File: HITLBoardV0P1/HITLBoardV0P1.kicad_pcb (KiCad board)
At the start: 2 copper layers, 37 parts, among them U1 TMDX570LC43HDK_Connectors, U2 LAN8650B1-E/LMX, U3 LP38852MRX-ADJ/NOPB

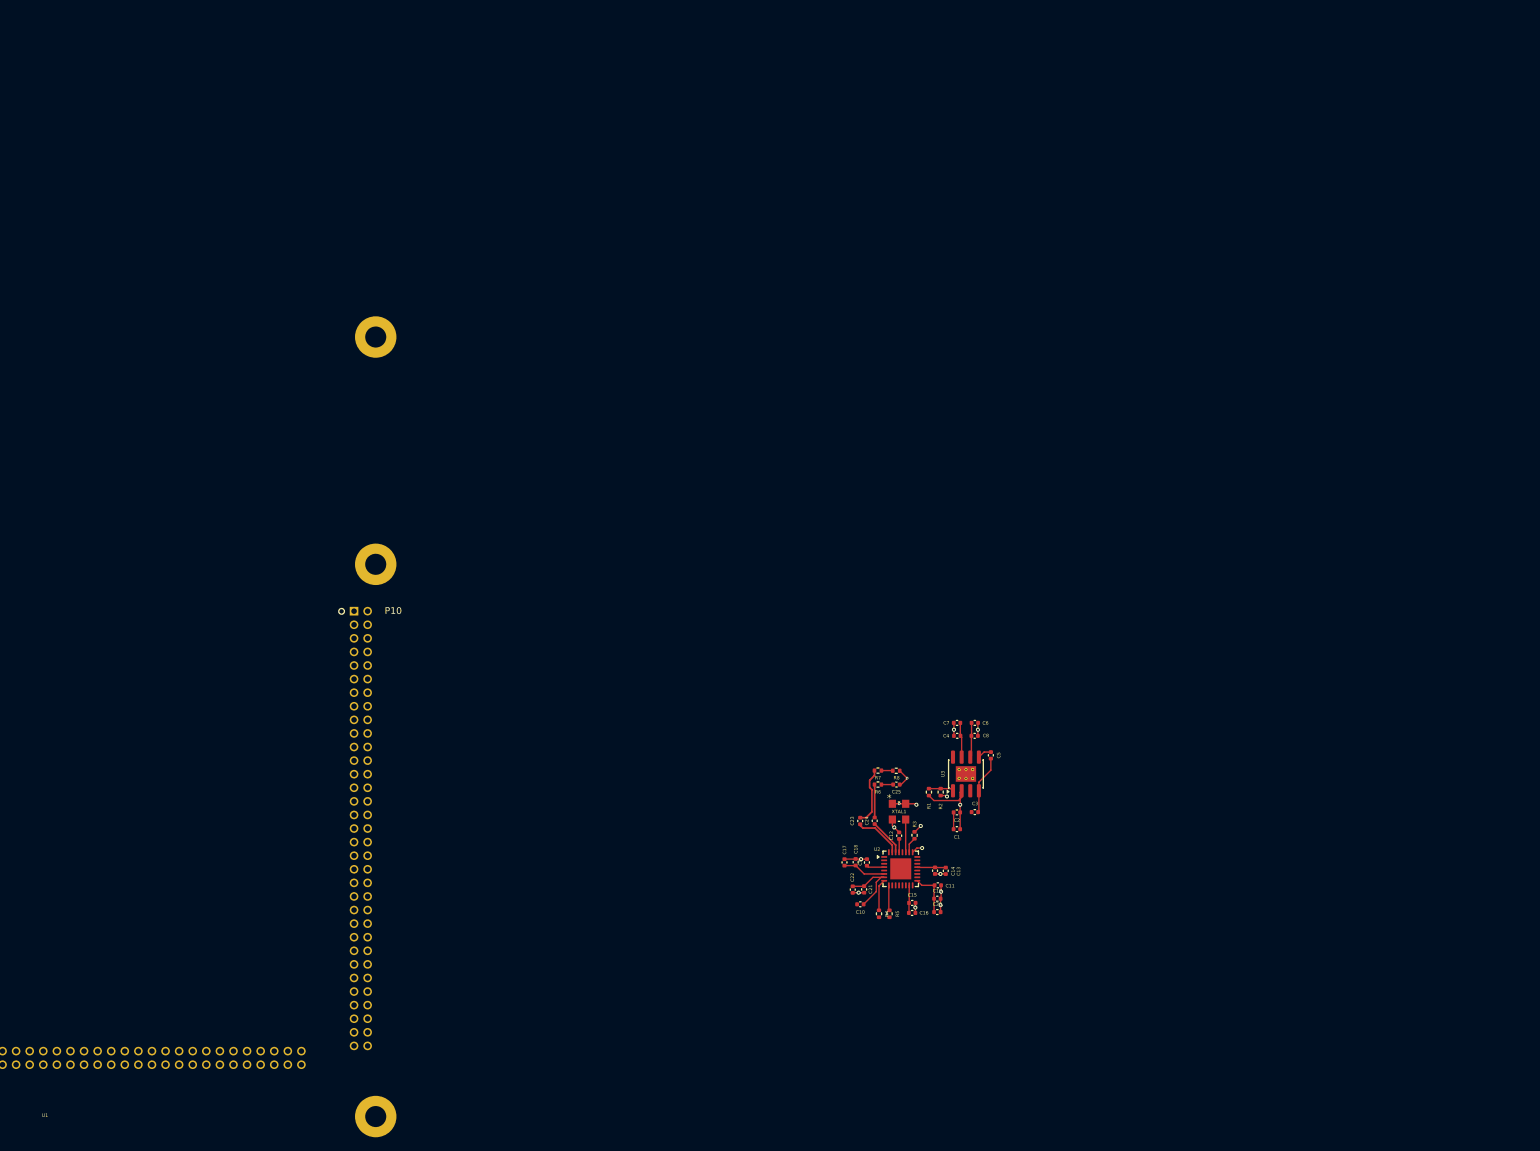
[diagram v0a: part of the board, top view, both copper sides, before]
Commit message: in progress, brute forced lan8650 layouts :( damn you kicad
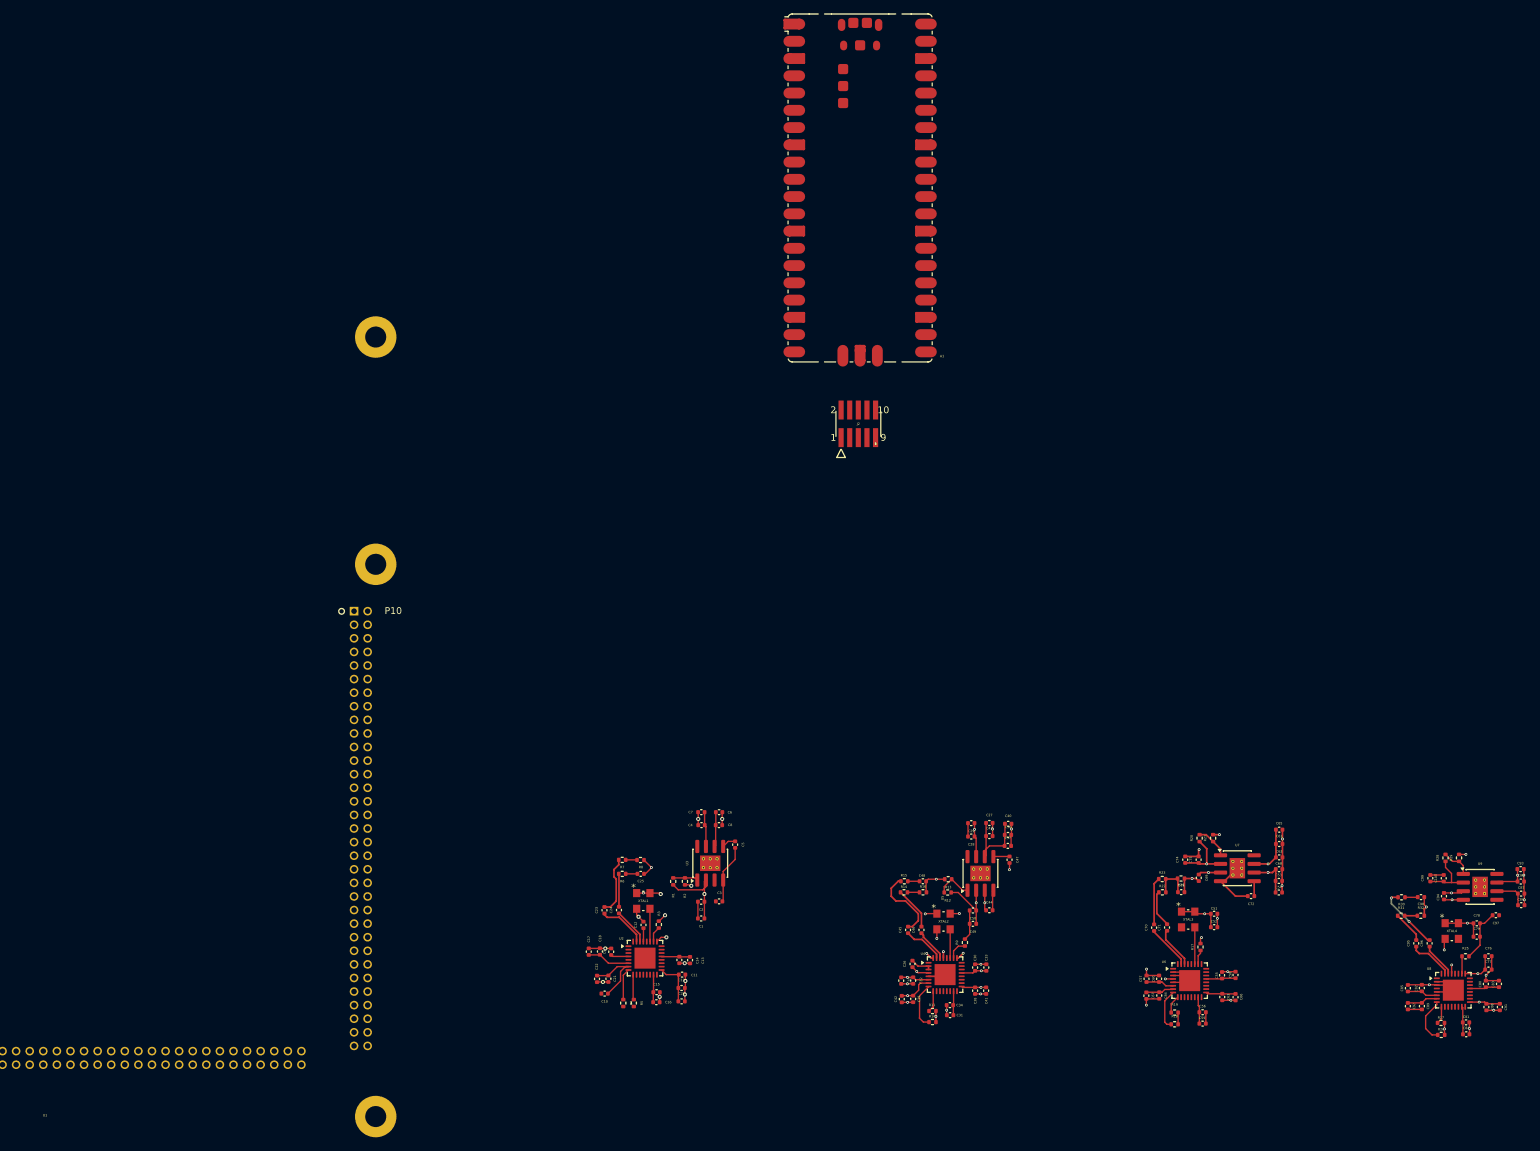
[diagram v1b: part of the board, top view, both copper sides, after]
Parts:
- added A1: RaspberryPi_Pico, Module:RaspberryPi_Pico_SMD, F.Cu at (295.7, 67.9)
- added C100: 1u, Capacitor_SMD:C_0402_1005Metric, F.Cu at (381.6, 169.6)
- added C26: 10u, Capacitor_SMD:C_0402_1005Metric, F.Cu at (303.4, 182.2)
- added C27: 10u, Capacitor_SMD:C_0402_1005Metric, F.Cu at (314.7, 161.4)
- added C28: 10u, Capacitor_SMD:C_0402_1005Metric, F.Cu at (312.1, 163.4)
- added C29: 10u, Capacitor_SMD:C_0402_1005Metric, F.Cu at (312.1, 161.5)
- added C30: 10n, Capacitor_SMD:C_0402_1005Metric, F.Cu at (312.6, 182.7)
- added C31: 10n, Capacitor_SMD:C_0402_1005Metric, F.Cu at (309.0, 189.7)
- added C32: 10n, Capacitor_SMD:C_0402_1005Metric, F.Cu at (303.5, 184.6)
- added C33: .1U, Capacitor_SMD:C_0402_1005Metric, F.Cu at (314.3, 182.7)
- added C34: .1U, Capacitor_SMD:C_0402_1005Metric, F.Cu at (308.9, 188.3)
- added C35: .1U, Capacitor_SMD:C_0402_1005Metric, F.Cu at (301.8, 184.6)
- added C36: 1u, Capacitor_SMD:C_0402_1005Metric, F.Cu at (317.5, 163.2)
- added C37: 1u, Capacitor_SMD:C_0402_1005Metric, F.Cu at (317.5, 164.8)
- added C38: 10n, Capacitor_SMD:C_0402_1005Metric, F.Cu at (312.6, 186.1)
- added C39: 10n, Capacitor_SMD:C_0402_1005Metric, F.Cu at (303.5, 187.3)
- added C40: 1u, Capacitor_SMD:C_0402_1005Metric, F.Cu at (317.5, 161.6)
- added C41: .1U, Capacitor_SMD:C_0402_1005Metric, F.Cu at (314.3, 186.1)
- added C42: .1U, Capacitor_SMD:C_0402_1005Metric, F.Cu at (301.9, 187.4)
- added C43: 1u, Capacitor_SMD:C_0402_1005Metric, F.Cu at (314.7, 163.4)
- added C44: 1u, Capacitor_SMD:C_0402_1005Metric, F.Cu at (314.7, 174.3)
- added C45: .1U, Capacitor_SMD:C_0402_1005Metric, F.Cu at (302.8, 177.2)
- added C46: .1U, Capacitor_SMD:C_0402_1005Metric, F.Cu at (304.7, 177.2)
- added C47: 1u, Capacitor_SMD:C_0402_1005Metric, F.Cu at (317.7, 166.8)
- added C48: .1U, Capacitor_SMD:C_0402_1005Metric, F.Cu at (305.0, 170.0)
- added C49: 100n, Capacitor_SMD:C_0402_1005Metric, F.Cu at (312.3, 176.3)
- added C50: 1u, Capacitor_SMD:C_0402_1005Metric, F.Cu at (312.3, 174.3)
- added C51: 10u, Capacitor_SMD:C_0402_1005Metric, F.Cu at (347.8, 174.8)
- added C52: 10u, Capacitor_SMD:C_0402_1005Metric, F.Cu at (347.8, 176.8)
- added C53: 10u, Capacitor_SMD:C_0402_1005Metric, F.Cu at (357.4, 170.0)
- added C54: 10u, Capacitor_SMD:C_0402_1005Metric, F.Cu at (357.4, 171.7)
- added C55: 10n, Capacitor_SMD:C_0402_1005Metric, F.Cu at (349.0, 183.9)
- added C56: 10n, Capacitor_SMD:C_0402_1005Metric, F.Cu at (346.1, 189.3)
- added C57: 10n, Capacitor_SMD:C_0402_1005Metric, F.Cu at (337.9, 184.4)
- added C58: .1U, Capacitor_SMD:C_0402_1005Metric, F.Cu at (351.0, 183.8)
- added C59: .1U, Capacitor_SMD:C_0402_1005Metric, F.Cu at (346.1, 191.0)
- added C60: .1U, Capacitor_SMD:C_0402_1005Metric, F.Cu at (339.7, 184.4)
- added C61: 1u, Capacitor_SMD:C_0402_1005Metric, F.Cu at (357.4, 164.5)
- added C62: 1u, Capacitor_SMD:C_0402_1005Metric, F.Cu at (357.4, 166.5)
- added C63: 10n, Capacitor_SMD:C_0402_1005Metric, F.Cu at (349.0, 187.1)
- added C64: 10n, Capacitor_SMD:C_0402_1005Metric, F.Cu at (339.8, 186.8)
- added C65: 1u, Capacitor_SMD:C_0402_1005Metric, F.Cu at (357.4, 162.4)
- added C66: .1U, Capacitor_SMD:C_0402_1005Metric, F.Cu at (351.0, 187.1)
- added C67: .1U, Capacitor_SMD:C_0402_1005Metric, F.Cu at (337.9, 186.9)
- added C68: 1u, Capacitor_SMD:C_0402_1005Metric, F.Cu at (357.4, 168.2)
- added C69: 1u, Capacitor_SMD:C_0402_1005Metric, F.Cu at (345.6, 169.5)
- added C70: .1U, Capacitor_SMD:C_0402_1005Metric, F.Cu at (339.0, 176.8)
- added C71: .1U, Capacitor_SMD:C_0402_1005Metric, F.Cu at (340.9, 176.8)
- added C72: 1u, Capacitor_SMD:C_0402_1005Metric, F.Cu at (353.3, 172.2)
- added C73: .1U, Capacitor_SMD:C_0402_1005Metric, F.Cu at (343.0, 171.6)
- added C74: 100n, Capacitor_SMD:C_0402_1005Metric, F.Cu at (343.6, 166.8)
- added C75: 1u, Capacitor_SMD:C_0402_1005Metric, F.Cu at (345.6, 166.8)
- added C76: 10u, Capacitor_SMD:C_0402_1005Metric, F.Cu at (388.2, 181.0)
- added C77: 10u, Capacitor_SMD:C_0402_1005Metric, F.Cu at (388.2, 183.0)
- added C78: 10u, Capacitor_SMD:C_0402_1005Metric, F.Cu at (386.5, 176.2)
- added C79: 10u, Capacitor_SMD:C_0402_1005Metric, F.Cu at (386.5, 178.2)
- added C80: 10n, Capacitor_SMD:C_0402_1005Metric, F.Cu at (387.8, 185.1)
- added C81: 10n, Capacitor_SMD:C_0402_1005Metric, F.Cu at (384.9, 190.8)
- added C82: 10n, Capacitor_SMD:C_0402_1005Metric, F.Cu at (378.4, 185.7)
- added C83: .1U, Capacitor_SMD:C_0402_1005Metric, F.Cu at (389.8, 185.1)
- added C84: .1U, Capacitor_SMD:C_0402_1005Metric, F.Cu at (384.9, 192.5)
- added C85: .1U, Capacitor_SMD:C_0402_1005Metric, F.Cu at (376.4, 185.8)
- added C86: 1u, Capacitor_SMD:C_0402_1005Metric, F.Cu at (393.1, 173.5)
- added C87: 1u, Capacitor_SMD:C_0402_1005Metric, F.Cu at (393.0, 171.8)
- added C88: 10n, Capacitor_SMD:C_0402_1005Metric, F.Cu at (387.9, 188.5)
- added C89: 10n, Capacitor_SMD:C_0402_1005Metric, F.Cu at (378.4, 188.4)
- added C90: 1u, Capacitor_SMD:C_0402_1005Metric, F.Cu at (393.0, 170.1)
- added C91: .1U, Capacitor_SMD:C_0402_1005Metric, F.Cu at (389.9, 188.5)
- added C92: .1U, Capacitor_SMD:C_0402_1005Metric, F.Cu at (376.4, 188.4)
- added C93: 1u, Capacitor_SMD:C_0402_1005Metric, F.Cu at (393.0, 168.2)
- added C94: 1u, Capacitor_SMD:C_0402_1005Metric, F.Cu at (381.7, 172.2)
- added C95: .1U, Capacitor_SMD:C_0402_1005Metric, F.Cu at (377.6, 179.2)
- added C96: .1U, Capacitor_SMD:C_0402_1005Metric, F.Cu at (379.6, 179.2)
- added C97: 1u, Capacitor_SMD:C_0402_1005Metric, F.Cu at (389.3, 175.0)
- added C98: .1U, Capacitor_SMD:C_0402_1005Metric, F.Cu at (378.3, 172.3)
- added C99: 100n, Capacitor_SMD:C_0402_1005Metric, F.Cu at (379.7, 169.6)
- added J2: FTSH-105-01-L-DV, GaladyneConnectorFootprintsLibrary:CON10_2X5_DU_FTSH_SAI, F.Cu at (295.5, 102.7)
- added R10: 10K, Resistor_SMD:R_0402_1005Metric, F.Cu at (306.4, 190.7)
- added R11: 10K, Resistor_SMD:R_0402_1005Metric, F.Cu at (306.4, 189.1)
- added R12: 2.94K, Resistor_SMD:R_0402_1005Metric, F.Cu at (308.6, 171.7)
- added R13: 1.13K, Resistor_SMD:R_0402_1005Metric, F.Cu at (308.7, 169.7)
- added R14: 49.9K, Resistor_SMD:R_0402_1005Metric, F.Cu at (302.2, 171.6)
- added R15: 49.9K, Resistor_SMD:R_0402_1005Metric, F.Cu at (302.2, 170.0)
- added R16: 100K, Resistor_SMD:R_0402_1005Metric, F.Cu at (305.0, 171.6)
- added R17: 12.4K, Resistor_SMD:R_0402_1005Metric, F.Cu at (345.8, 179.7)
- added R18: 10K, Resistor_SMD:R_0402_1005Metric, F.Cu at (342.0, 191.1)
- added R19: 10K, Resistor_SMD:R_0402_1005Metric, F.Cu at (342.0, 189.3)
- added R20: 2.94K, Resistor_SMD:R_0402_1005Metric, F.Cu at (345.7, 163.7)
- added R21: 1.13K, Resistor_SMD:R_0402_1005Metric, F.Cu at (347.7, 163.7)
- added R22: 49.9K, Resistor_SMD:R_0402_1005Metric, F.Cu at (340.2, 171.6)
- added R23: 49.9K, Resistor_SMD:R_0402_1005Metric, F.Cu at (340.2, 169.7)
- added R24: 100K, Resistor_SMD:R_0402_1005Metric, F.Cu at (343.0, 169.6)
- added R25: 12.4K, Resistor_SMD:R_0402_1005Metric, F.Cu at (384.8, 181.1)
- added R26: 10K, Resistor_SMD:R_0402_1005Metric, F.Cu at (381.3, 192.6)
- added R27: 10K, Resistor_SMD:R_0402_1005Metric, F.Cu at (381.2, 190.9)
- added R28: 2.94K, Resistor_SMD:R_0402_1005Metric, F.Cu at (381.9, 166.6)
- added R29: 1.13K, Resistor_SMD:R_0402_1005Metric, F.Cu at (383.9, 166.6)
- added R30: 49.9K, Resistor_SMD:R_0402_1005Metric, F.Cu at (375.4, 172.4)
- added R31: 49.9K, Resistor_SMD:R_0402_1005Metric, F.Cu at (375.4, 175.1)
- added R32: 100K, Resistor_SMD:R_0402_1005Metric, F.Cu at (378.3, 175.1)
- added R9: 12.4K, Resistor_SMD:R_0402_1005Metric, F.Cu at (311.1, 179.0)
- added U4: LAN8650B1-E/LMX, Package_DFN_QFN:QFN-32-1EP_5x5mm_P0.5mm_EP3.1x3.1mm, F.Cu at (308.2, 183.8)
- added U5: LP38852MRX-ADJ/NOPB, Package_SO:SOIC-8-1EP_3.9x4.9mm_P1.27mm_EP2.29x3mm_ThermalVias, F.Cu at (313.4, 168.9)
- added U6: LAN8650B1-E/LMX, Package_DFN_QFN:QFN-32-1EP_5x5mm_P0.5mm_EP3.1x3.1mm, F.Cu at (344.2, 184.6)
- added U7: LP38852MRX-ADJ/NOPB, Package_SO:SOIC-8-1EP_3.9x4.9mm_P1.27mm_EP2.29x3mm_ThermalVias, F.Cu at (351.3, 168.1)
- added U8: LAN8650B1-E/LMX, Package_DFN_QFN:QFN-32-1EP_5x5mm_P0.5mm_EP3.1x3.1mm, F.Cu at (383.1, 186.1)
- added U9: LP38852MRX-ADJ/NOPB, Package_SO:SOIC-8-1EP_3.9x4.9mm_P1.27mm_EP2.29x3mm_ThermalVias, F.Cu at (387.0, 170.8)
- added XTAL2: ECS-2520S33-250-FN-TR, GaladyneOscillatorFootprintsLibrary:ECS-2520S_ECS, F.Cu at (308.0, 175.9)
- added XTAL3: ECS-2520S33-250-FN-TR, GaladyneOscillatorFootprintsLibrary:ECS-2520S_ECS, F.Cu at (344.0, 175.6)
- added XTAL4: ECS-2520S33-250-FN-TR, GaladyneOscillatorFootprintsLibrary:ECS-2520S_ECS, F.Cu at (382.8, 177.3)
- C1: value 100n -> 10u
- C10, C9: value 10u -> .1U
- C11, C12: value 10u -> 1u
- C14: value .1U -> 10n
- C15, C19: value 10n -> 1u
- C17, C21: value 10n -> .1U
- C18, C22, C25: value .1U -> 1u
- C2, C3, C4: value 1u -> 10u
- C24: value .1U -> 100n
- C5, C6, C7: value 1u -> 10n
- C8: value 1u -> .1U
- R1: value 2.94K -> 12.4K
- R2: value 1.13K -> 10K
- R3: value 12.4K -> 10K
- R4: value 10K -> 2.94K
- R5: value 10K -> 1.13K
- moved C18 39.9 mm to (257.4, 180.4)
- moved C25 39.9 mm to (263.4, 168.9)
- moved R6 39.9 mm to (260.7, 168.9)
- moved R4 39.9 mm to (260.9, 187.9)
- moved R5 39.9 mm to (262.4, 187.9)
- moved C1 39.9 mm to (272.3, 175.5)
- moved C10 39.9 mm to (258.1, 186.6)
- moved C11 39.9 mm to (269.5, 183.8)
- moved C13 39.9 mm to (270.7, 181.6)
- moved C14 39.9 mm to (269.1, 181.6)
- moved C15 39.9 mm to (265.8, 186.3)
- moved C17 39.9 mm to (255.8, 180.4)
- moved C19 39.9 mm to (269.4, 185.7)
- moved C2 39.9 mm to (272.3, 173.0)
- moved C20 39.9 mm to (269.4, 187.7)
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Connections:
- C1 pad 1: /Ethernet/1V8_U2 -> +3V3
- C13 pad 1: /Ethernet/1V8_U2 -> +3V3
- C14 pad 1: /Ethernet/1V8_U2 -> +3V3
- C15 pad 1: /Ethernet/1V8_U2 -> +3V3
- C16 pad 1: /Ethernet/1V8_U2 -> +3V3
- C17 pad 1: /Ethernet/1V8_U2 -> +3V3
- C18 pad 1: /Ethernet/1V8_U2 -> +3V3
- C19 pad 1: +3V3 -> +5V
- C2 pad 1: /Ethernet/1V8_U2 -> +3V3
- C20 pad 1: +3V3 -> /Ethernet/TRXN
- C20 pad 2: GND -> /Ethernet/ETH_10T1S_TRXN
- C21 pad 1: +3V3 -> /Ethernet/TRXP
- C21 pad 2: GND -> /Ethernet/ETH_10T1S_TRXP
- C22 pad 1: +3V3 -> /Ethernet/U3_SS
- C23 pad 1: /Ethernet/TRXN_N -> GND
- C23 pad 2: /Ethernet/ETH_10T1S_TRXN_N -> Net-(C23-Pad2)
- C24 pad 1: /Ethernet/TRXP_P -> /Ethernet/1V8_U2
- C24 pad 2: /Ethernet/ETH_10T1S_TRXP_P -> GND
- C25 pad 1: GND -> /Ethernet/1V8_U2
- C25 pad 2: Net-(C25-Pad2) -> GND
- C3 pad 1: +5V -> +3V3
- C5 pad 1: /Ethernet/U3_SS -> +3V3
- R1 pad 1: /Ethernet/1V8_U2 -> /Ethernet/BIAS
- R1 pad 2: /Ethernet/U3_ADJ -> GND
- R2 pad 1: /Ethernet/U3_ADJ -> /Ethernet/RESET_N
- R2 pad 2: GND -> +3V3
- R3 pad 1: /Ethernet/BIAS -> /Ethernet/IRQ_N
- R3 pad 2: GND -> +3V3
- R4 pad 1: /Ethernet/RESET_N -> /Ethernet/1V8_U2
- R4 pad 2: +3V3 -> /Ethernet/U3_ADJ
- R5 pad 1: /Ethernet/IRQ_N -> /Ethernet/U3_ADJ
- R5 pad 2: +3V3 -> GND
- R6 pad 1: /Ethernet/ETH_10T1S_TRXP_P -> /Ethernet/ETH_10T1S_TRXP
- R6 pad 2: Net-(C25-Pad2) -> Net-(C23-Pad2)
- R7 pad 1: /Ethernet/ETH_10T1S_TRXN_N -> /Ethernet/ETH_10T1S_TRXN
- R7 pad 2: Net-(C25-Pad2) -> Net-(C23-Pad2)
- R8 pad 1: Net-(C25-Pad2) -> Net-(C23-Pad2)
- U1 pad P10-1: unconnected-(U1B-EXP_12V-PadP10-1) -> +12V
- U1 pad P10-29: unconnected-(U1B-GND-PadP10-29) -> GND
- U1 pad P10-30: unconnected-(U1B-GND-PadP10-30) -> GND
- U1 pad P10-39: unconnected-(U1B-GND-PadP10-39) -> GND
- U1 pad P10-40: unconnected-(U1B-GND-PadP10-40) -> GND
- U1 pad P10-57: unconnected-(U1B-GND-PadP10-57) -> GND
- U1 pad P10-58: unconnected-(U1B-GND-PadP10-58) -> GND
- U1 pad P10-65: unconnected-(U1B-EXP_12V-PadP10-65) -> +12V
- U1 pad P10-66: unconnected-(U1B-GND-PadP10-66) -> GND
- U1 pad P11-1: unconnected-(U1C-EXP_12V-PadP11-1) -> +12V
- U1 pad P11-19: unconnected-(U1C-GIOA_1-PadP11-19) -> /TMDX_Breakout/GIOA_1
- U1 pad P11-21: unconnected-(U1C-GIOA_3-PadP11-21) -> /TMDX_Breakout/GIOA_3
- U1 pad P11-23: unconnected-(U1C-GIOA_5-PadP11-23) -> /TMDX_Breakout/GIOA_5
- U1 pad P11-25: unconnected-(U1C-GIOA_7-PadP11-25) -> /TMDX_Breakout/GIOA_7
- U1 pad P11-27: unconnected-(U1C-GIOB_1-PadP11-27) -> /TMDX_Breakout/GIOB_1
- U1 pad P11-29: unconnected-(U1C-GIOB_3-PadP11-29) -> /TMDX_Breakout/GIOB_3
- U1 pad P11-3: unconnected-(U1C-EXP_12V-PadP11-3) -> +12V
- U1 pad P11-31: unconnected-(U1C-GIOB_5-PadP11-31) -> /TMDX_Breakout/GIOB_5
- U1 pad P9-1: unconnected-(U1A-EXP_12V-PadP9-1) -> +12V
- U1 pad P9-13: unconnected-(U1A-GND-PadP9-13) -> GND
- U1 pad P9-14: unconnected-(U1A-GND-PadP9-14) -> GND
- U1 pad P9-2: unconnected-(U1A-GND-PadP9-2) -> GND
- U1 pad P9-29: unconnected-(U1A-GND-PadP9-29) -> GND
- U1 pad P9-3: unconnected-(U1A-EXP_12V-PadP9-3) -> +12V
- U1 pad P9-30: unconnected-(U1A-GND-PadP9-30) -> GND
- U1 pad P9-39: unconnected-(U1A-GND-PadP9-39) -> GND
- U1 pad P9-4: unconnected-(U1A-GND-PadP9-4) -> GND
- U1 pad P9-40: unconnected-(U1A-GND-PadP9-40) -> GND
- U1 pad P9-49: unconnected-(U1A-GND-PadP9-49) -> GND
- U1 pad P9-50: unconnected-(U1A-GND-PadP9-50) -> GND
- U1 pad P9-59: unconnected-(U1A-GND-PadP9-59) -> GND
- U1 pad P9-65: unconnected-(U1A-EXP_12V-PadP9-65) -> +12V
- U1 pad P9-66: unconnected-(U1A-GND-PadP9-66) -> GND
- U2 pad 30: /Ethernet/TRXP_P -> /Ethernet/TRXP
- U2 pad 31: /Ethernet/TRXN_N -> /Ethernet/TRXN
- U3 pad 9: GND -> /Ethernet/U3_DAP
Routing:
- net GND: track 34.8 -> 164.7 mm, vias 12 -> 41
- net +3V3: track 37.6 -> 141.3 mm, vias 3 -> 24
- net (no net): track 0.00 -> 27.8 mm
- net /ethernet3/1V8: track 0.00 -> 21.5 mm, vias 0 -> 1
- net /ethernet4/1V8: track 0.00 -> 21.4 mm
- net /Ethernet2/1V8: track 0.00 -> 21.2 mm, vias 0 -> 3
- net /Ethernet2/ETH_10T1S_TRXN: track 0.00 -> 11.0 mm
- net /ethernet4/ETH_10T1S_TRXP: track 0.00 -> 9.73 mm, vias 0 -> 2
- net +5V: track 0.00 -> 9.30 mm, vias 0 -> 3
- net /Ethernet/ETH_10T1S_TRXN_N: track 8.59 -> 0.00 mm
- net /Ethernet/TRXN_N: track 7.15 -> 0.00 mm
- net /ethernet3/ETH_10T1S_TRXN: track 0.00 -> 6.96 mm
- net /LAN_RESET_N_1: track 0.00 -> 6.87 mm
- net /ethernet4/RESET_N: track 0.00 -> 6.74 mm
- net /ethernet3/TRXN: track 0.00 -> 6.53 mm
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
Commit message: update
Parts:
- added C101: 100p, Capacitor_SMD:C_0402_1005Metric, F.Cu at (343.1, 124.1)
- added C102: 0.1u, Capacitor_SMD:C_0402_1005Metric, F.Cu at (341.1, 124.1)
- added C103: 0.1u, Capacitor_SMD:C_0402_1005Metric, F.Cu at (337.3, 129.1)
- added C104: 0.1u, Capacitor_SMD:C_0402_1005Metric, F.Cu at (329.3, 132.6)
- added C105: 0.1u, Capacitor_SMD:C_0402_1005Metric, F.Cu at (335.0, 132.4)
- added C106: 0.1u, Capacitor_SMD:C_0402_1005Metric, F.Cu at (342.8, 138.5)
- added C107: 0.1u, Capacitor_SMD:C_0402_1005Metric, F.Cu at (353.6, 134.8)
- added R33: 10, Resistor_SMD:R_1206_3216Metric, F.Cu at (345.9, 125.0)
- added R34: 15, Resistor_SMD:R_1206_3216Metric, F.Cu at (352.6, 132.2)
- added R35: 15K, Resistor_SMD:R_0402_1005Metric, F.Cu at (345.9, 138.7)
- added U10: DAC7750IPWPR, GaladyneIntegratedCircuitsFootprintsLibrary:PWP24_TEX, F.Cu at (343.0, 132.5)
- added U11: NC7SZ04P5X, GaladyneIntegratedCircuitsFootprintsLibrary:SC-88A-5_1P35X2P2_ONS, F.Cu at (328.8, 135.3)
- added U12: SN74LVC1G08DCKR, GaladyneIntegratedCircuitsFootprintsLibrary:DCK5, F.Cu at (334.1, 135.3)
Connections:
- net /Ethernet2/ETH_10T1S_TRXN renamed /ETH_10T1S_A_TRXN
- net /Ethernet2/ETH_10T1S_TRXP renamed /ETH_10T1S_A_TRXP
- C70 pad 2: /ethernet3/ETH_10T1S_TRXN -> /ETH_10T1S_B_TRXN
- C71 pad 2: /ethernet3/ETH_10T1S_TRXP -> /ETH_10T1S_B_TRXP
- C95 pad 2: /ethernet4/ETH_10T1S_TRXN -> /ETH_10T1S_B_TRXN
- C96 pad 2: /ethernet4/ETH_10T1S_TRXP -> /ETH_10T1S_B_TRXP
- R22 pad 1: /ethernet3/ETH_10T1S_TRXP -> /ETH_10T1S_B_TRXP
- R23 pad 1: /ethernet3/ETH_10T1S_TRXN -> /ETH_10T1S_B_TRXN
- R30 pad 1: /ethernet4/ETH_10T1S_TRXP -> /ETH_10T1S_B_TRXP
- R31 pad 1: /ethernet4/ETH_10T1S_TRXN -> /ETH_10T1S_B_TRXN
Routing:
- net /ETH_10T1S_B_TRXP: track 0.00 -> 15.2 mm, vias 0 -> 2
- net GND: track 164.7 -> 179.6 mm, vias 41 -> 50
- net /ETH_10T1S_B_TRXN: track 0.00 -> 11.7 mm
- net /ethernet4/ETH_10T1S_TRXP: track 9.73 -> 0.00 mm, vias 2 -> 0
- net +3.3VP: track 0.00 -> 8.27 mm, vias 0 -> 2
- net /ethernet3/ETH_10T1S_TRXN: track 6.96 -> 0.00 mm
- net /DAC/SCLK_AND_LATCH_N: track 0.00 -> 5.97 mm
- net /DAC/REFOUT: track 0.00 -> 5.56 mm
- net /ethernet3/ETH_10T1S_TRXP: track 5.45 -> 0.00 mm
- net /DAC/IOUT: track 0.00 -> 5.21 mm
- net +12V: track 0.00 -> 4.84 mm
- net /ethernet4/ETH_10T1S_TRXN: track 4.71 -> 0.00 mm
- net /DAC/LATCH_N: track 0.00 -> 3.84 mm
- net /DAC/CURRENT_OUT: track 0.00 -> 2.62 mm
- net /DAC/AVDD: track 0.00 -> 2.45 mm
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
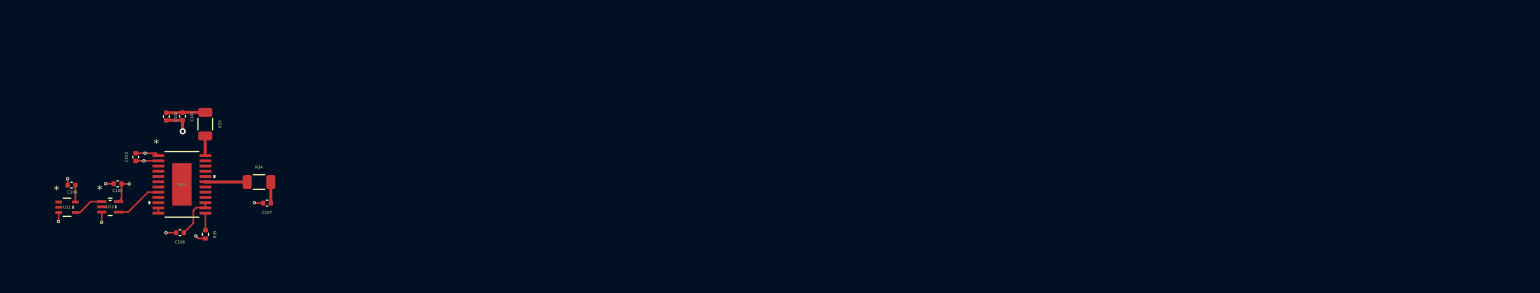
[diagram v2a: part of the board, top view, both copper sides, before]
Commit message: UPDATE IN PROGRESS, 4 DACS ADDED AND INITIAL ROUTED IN PCB
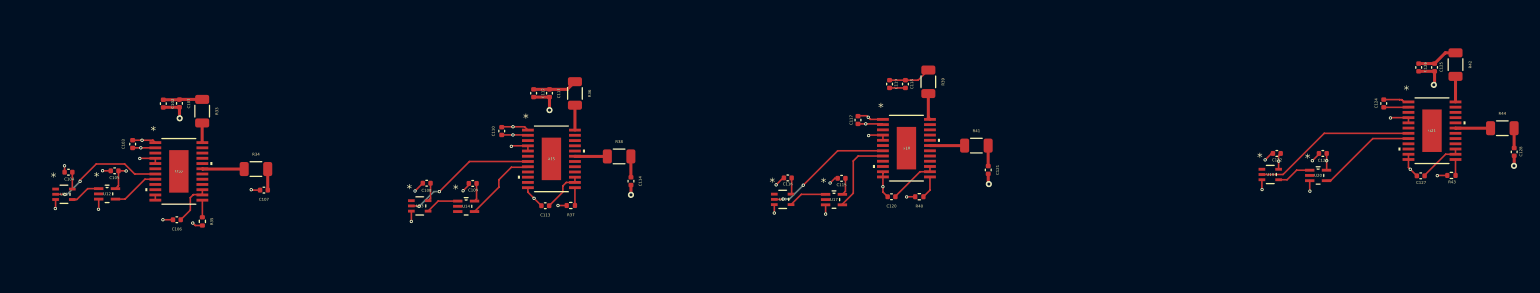
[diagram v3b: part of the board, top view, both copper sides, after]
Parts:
- added C108: 0.1u, Capacitor_SMD:C_0402_1005Metric, F.Cu at (373.4, 132.4)
- added C109: 0.1u, Capacitor_SMD:C_0402_1005Metric, F.Cu at (379.1, 132.4)
- added C110: 0.1u, Capacitor_SMD:C_0402_1005Metric, F.Cu at (382.8, 125.9)
- added C111: 100p, Capacitor_SMD:C_0402_1005Metric, F.Cu at (388.7, 121.2)
- added C112: 0.1u, Capacitor_SMD:C_0402_1005Metric, F.Cu at (386.7, 121.2)
- added C113: 0.1u, Capacitor_SMD:C_0402_1005Metric, F.Cu at (388.2, 135.2)
- added C114: 0.1u, Capacitor_SMD:C_0402_1005Metric, F.Cu at (398.8, 132.1)
- added C115: 0.1u, Capacitor_SMD:C_0402_1005Metric, F.Cu at (425.0, 131.8)
- added C116: 0.1u, Capacitor_SMD:C_0402_1005Metric, F.Cu at (418.3, 131.7)
- added C117: 0.1u, Capacitor_SMD:C_0402_1005Metric, F.Cu at (427.0, 124.5)
- added C118: 100p, Capacitor_SMD:C_0402_1005Metric, F.Cu at (432.9, 120.0)
- added C119: 0.1u, Capacitor_SMD:C_0402_1005Metric, F.Cu at (430.9, 120.0)
- added C120: 0.1u, Capacitor_SMD:C_0402_1005Metric, F.Cu at (431.2, 134.0)
- added C121: 0.1u, Capacitor_SMD:C_0402_1005Metric, F.Cu at (443.2, 130.7)
- added C122: 0.1u, Capacitor_SMD:C_0402_1005Metric, F.Cu at (479.0, 128.7)
- added C123: 0.1u, Capacitor_SMD:C_0402_1005Metric, F.Cu at (484.7, 128.7)
- added C124: 0.1u, Capacitor_SMD:C_0402_1005Metric, F.Cu at (492.3, 122.5)
- added C125: 100p, Capacitor_SMD:C_0402_1005Metric, F.Cu at (498.6, 118.0)
- added C126: 0.1u, Capacitor_SMD:C_0402_1005Metric, F.Cu at (496.6, 118.0)
- added C127: 0.1u, Capacitor_SMD:C_0402_1005Metric, F.Cu at (496.9, 131.4)
- added C128: 0.1u, Capacitor_SMD:C_0402_1005Metric, F.Cu at (508.5, 128.5)
- added R36: 10, Resistor_SMD:R_1206_3216Metric, F.Cu at (391.8, 121.2)
- added R37: 15K, Resistor_SMD:R_0402_1005Metric, F.Cu at (391.3, 135.1)
- added R38: 15, Resistor_SMD:R_1206_3216Metric, F.Cu at (397.3, 129.0)
- added R39: 10, Resistor_SMD:R_1206_3216Metric, F.Cu at (435.7, 119.8)
- added R40: 15K, Resistor_SMD:R_0402_1005Metric, F.Cu at (434.6, 134.0)
- added R41: 15, Resistor_SMD:R_1206_3216Metric, F.Cu at (441.7, 127.7)
- added R42: 10, Resistor_SMD:R_1206_3216Metric, F.Cu at (501.2, 117.6)
- added R43: 15K, Resistor_SMD:R_0402_1005Metric, F.Cu at (500.7, 131.4)
- added R44: 15, Resistor_SMD:R_1206_3216Metric, F.Cu at (507.0, 125.5)
- added U13: NC7SZ04P5X, GaladyneIntegratedCircuitsFootprintsLibrary:SC-88A-5_1P35X2P2_ONS, F.Cu at (372.6, 135.2)
- added U14: SN74LVC1G08DCKR, GaladyneIntegratedCircuitsFootprintsLibrary:DCK5, F.Cu at (378.3, 135.2)
- added U15: DAC7750IPWPR, GaladyneIntegratedCircuitsFootprintsLibrary:PWP24_TEX, F.Cu at (388.9, 129.3)
- added U16: NC7SZ04P5X, GaladyneIntegratedCircuitsFootprintsLibrary:SC-88A-5_1P35X2P2_ONS, F.Cu at (417.6, 134.4)
- added U17: SN74LVC1G08DCKR, GaladyneIntegratedCircuitsFootprintsLibrary:DCK5, F.Cu at (424.0, 134.4)
- added U18: DAC7750IPWPR, GaladyneIntegratedCircuitsFootprintsLibrary:PWP24_TEX, F.Cu at (433.0, 128.0)
- added U19: NC7SZ04P5X, GaladyneIntegratedCircuitsFootprintsLibrary:SC-88A-5_1P35X2P2_ONS, F.Cu at (478.2, 131.3)
- added U20: SN74LVC1G08DCKR, GaladyneIntegratedCircuitsFootprintsLibrary:DCK5, F.Cu at (484.2, 131.4)
- added U21: DAC7750IPWPR, GaladyneIntegratedCircuitsFootprintsLibrary:PWP24_TEX, F.Cu at (498.3, 125.8)
- moved C104 1.66 mm to (328.9, 131.0)
- moved R34 1.66 mm to (352.2, 130.6)
- moved U11 1.66 mm to (328.4, 133.7)
- moved C105 1.66 mm to (334.7, 130.8)
- moved U10 1.66 mm to (342.6, 130.9)
- moved C101 1.66 mm to (342.7, 122.4)
- moved C102 1.66 mm to (340.7, 122.5)
- moved C103 1.66 mm to (336.9, 127.5)
- moved R33 1.66 mm to (345.5, 123.4)
- moved U12 1.66 mm to (333.7, 133.7)
- moved C106 1.66 mm to (342.4, 136.9)
- moved C107 1.66 mm to (353.2, 133.2)
- moved R35 1.66 mm to (345.6, 137.1)
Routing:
- net GND: track 179.6 -> 240.0 mm, vias 50 -> 78
- net +3.3VP: track 8.27 -> 30.7 mm, vias 2 -> 6
- net /dac4/LATCH: track 0.00 -> 20.3 mm
- net /dac2/LATCH: track 0.00 -> 16.8 mm, vias 0 -> 2
- net /dac3/LATCH: track 0.00 -> 16.0 mm, vias 0 -> 2
- net +12V: track 4.84 -> 20.8 mm
- net /DAC/LATCH: track 0.00 -> 14.6 mm, vias 0 -> 2
- net /dac4/SCLK_AND_LATCH_N: track 0.00 -> 12.3 mm
- net /dac3/SCLK_AND_LATCH_N: track 0.00 -> 9.95 mm
- net /dac2/SCLK_AND_LATCH_N: track 0.00 -> 9.48 mm
- net /dac3/REFOUT: track 0.00 -> 6.26 mm
- net /dac4/REFOUT: track 0.00 -> 5.64 mm
- net /dac2/REFOUT: track 0.00 -> 5.50 mm
- net /dac3/LATCH_N: track 0.00 -> 4.82 mm
- net /dac4/IOUT: track 0.00 -> 4.36 mm
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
